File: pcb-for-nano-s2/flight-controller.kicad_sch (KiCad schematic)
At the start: 53 parts, among them J1 BM03B-SRSS-TBLFSN, J2 BM03B-SRSS-TBLFSN, J3 BM03B-SRSS-TBLFSN, J4 Conn_01x02, J5 Conn_ARM_JTAG_SWD_10, J6 Conn_01x02, Q1 Q_NMOS_GSD, Q2 Q_NMOS_GSD, U1 STM32G4A1KEU6, U2 ZOE-M8Q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

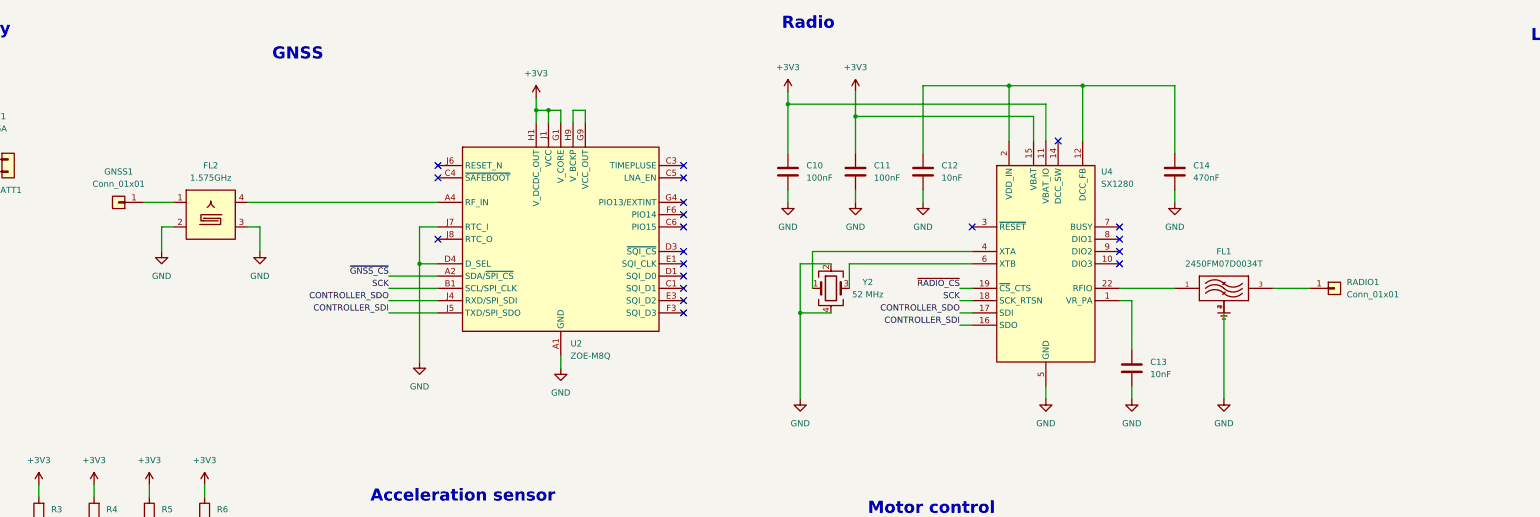
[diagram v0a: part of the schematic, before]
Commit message: add impedance matching circuits for antennas
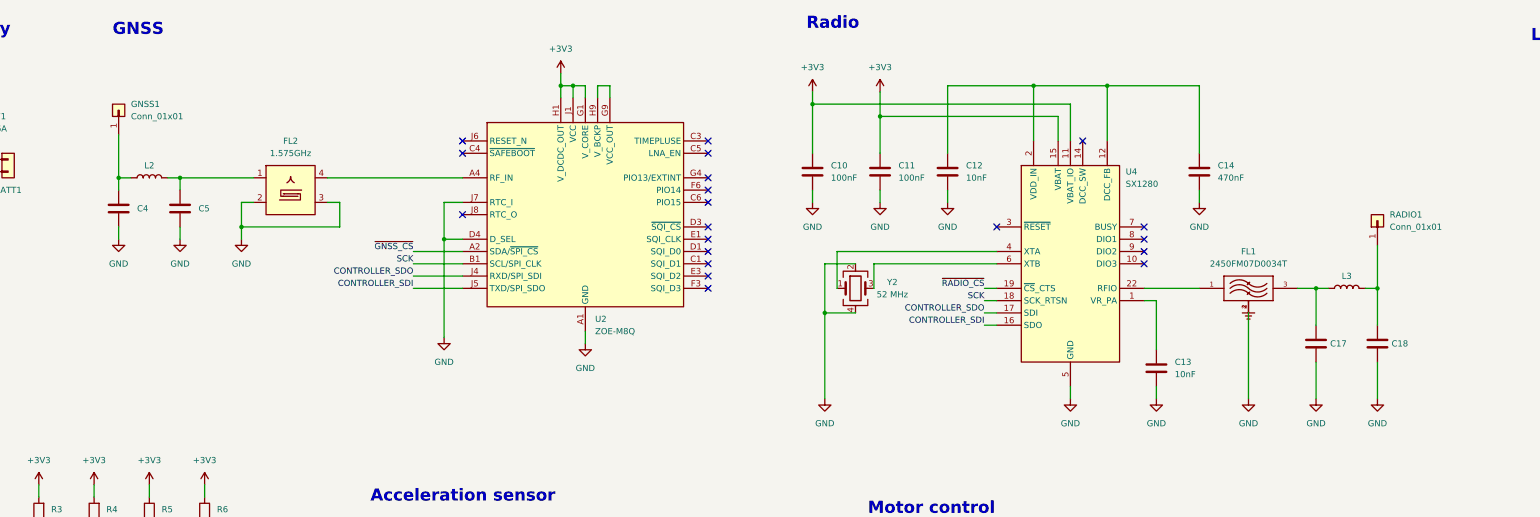
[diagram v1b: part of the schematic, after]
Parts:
- added C17, C18, C4, C5: ~, Capacitor_SMD:C_0402_1005Metric, symbol Device:C
- added L2, L3: ~, Inductor_SMD:L_0402_1005Metric, symbol Device:L
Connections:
- net GND: now also C17.1, C18.1, C4.1, C5.1
- net at FL2.1: now also C5.2, L2.2; no longer GNSS1.1 (Pin_1)
- net at RADIO1.1 (Pin_1): now also C18.2, L3.2; no longer FL1.3
- new net: C17.2, FL1.3, L3.1
- new net: C4.2, GNSS1.1 (Pin_1), L2.1
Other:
- moved on the sheet: C10, C11, C12, C13, C14, FL1, FL2, GNSS1, RADIO1, U2, U4, Y2

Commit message: fix component infos
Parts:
- BATT1, GNSS1, RADIO1: now left out of the parts list
- C1, C2: MPN GRM155R60J106ME15 -> GRM155R60J106ME15D
- C15, C16: MPN GRM188R60J476ME15 -> GRM188R60J476ME15D
- J1, J2, J3: MPN BM03B-SRSS-TB -> CI1103M1VR0-NH
- J6: MPN (none) -> 0530470210
- U3: MPN LSM6DSR -> LSM6DSRTR
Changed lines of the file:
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@@
       (effects (font (size 1.27 1.27)) hide)
     )
-    (property "MPN" "GRM188R60J476ME15" (id 4) (at 215.9 255.27 0)
+    (property "MPN" "GRM188R60J476ME15D" (id 4) (at 215.9 255.27 0)
       (effects (font (size 1.27 1.27)) hide)
     )
@@
       (effects (font (size 1.27 1.27)) hide)
     )
-    (property "MPN" "BM03B-SRSS-TB" (id 4) (at 375.92 132.08 0)
+    (property "MPN" "CI1103M1VR0-NH" (id 4) (at 375.92 132.08 0)
       (effects (font (size 1.27 1.27)) hide)
     )
@@
       (effects (font (size 1.27 1.27)) hide)
     )
-    (property "MPN" "GRM188R60J476ME15" (id 4) (at 278.13 246.38 0)
+    (property "MPN" "GRM188R60J476ME15D" (id 4) (at 278.13 246.38 0)
       (effects (font (size 1.27 1.27)) hide)
     )
@@
       (effects (font (size 1.27 1.27)) hide)
     )
-    (property "MPN" "BM03B-SRSS-TB" (id 4) (at 375.92 161.29 0)
+    (property "MPN" "CI1103M1VR0-NH" (id 4) (at 375.92 161.29 0)
       (effects (font (size 1.27 1.27)) hide)
     )
@@
   )
   (symbol (lib_id "Connector_Generic:Conn_01x01") (at 59.69 41.91 90) (unit 1)
-    (in_bom yes) (on_board yes) (fields_autoplaced)
+    (in_bom no) (on_board yes) (fields_autoplaced)
     (property "Reference" "GNSS1" (id 0) (at 62.23 40.6399 90)
       (effects (font (size 1.27 1.27)) (justify right))
@@
       (effects (font (size 1.27 1.27)) hide)
     )
-    (property "MPN" "GRM155R60J106ME15" (id 4) (at 25.4 193.04 0)
+    (property "MPN" "GRM155R60J106ME15D" (id 4) (at 25.4 193.04 0)
       (effects (font (size 1.27 1.27)) hide)
     )
@@
     )
     (property "Datasheet" "~" (id 3) (at 283.21 151.13 0)
+      (effects (font (size 1.27 1.27)) hide)
+    )
+    (property "MPN" "0530470210" (id 4) (at 283.21 151.13 0)
       (effects (font (size 1.27 1.27)) hide)
     )
@@
       (effects (font (size 1.27 1.27)) hide)
     )
-    (property "MPN" "GRM155R60J106ME15" (id 4) (at 38.1 193.04 0)
+    (property "MPN" "GRM155R60J106ME15D" (id 4) (at 38.1 193.04 0)
       (effects (font (size 1.27 1.27)) hide)
     )
@@
   )
   (symbol (lib_id "Connector_Generic:Conn_01x01") (at 320.04 64.77 90) (unit 1)
-    (in_bom yes) (on_board yes) (fields_autoplaced)
+    (in_bom no) (on_board yes) (fields_autoplaced)
     (property "Reference" "RADIO1" (id 0) (at 322.58 63.4999 90)
       (effects (font (size 1.27 1.27)) (justify right))
@@
       (effects (font (size 1.27 1.27)) hide)
     )
-    (property "MPN" "BM03B-SRSS-TB" (id 4) (at 375.92 102.87 0)
+    (property "MPN" "CI1103M1VR0-NH" (id 4) (at 375.92 102.87 0)
       (effects (font (size 1.27 1.27)) hide)
     )
@@
   )
   (symbol (lib_id "Connector_Generic:Conn_01x02") (at 36.83 52.07 0) (unit 1)
-    (in_bom yes) (on_board yes)
+    (in_bom no) (on_board yes)
     (property "Reference" "BATT1" (id 0) (at 36.83 58.42 0))
     (property "Value" "Conn_01x02" (id 1) (at 36.83 58.42 0)
@@
       (effects (font (size 1.27 1.27)) (justify left) hide)
     )
-    (property "MPN" "LSM6DSR" (id 29) (at 147.32 175.26 0)
+    (property "MPN" "LSM6DSRTR" (id 29) (at 147.32 175.26 0)
       (effects (font (size 1.27 1.27)) (justify left) hide)
     )
